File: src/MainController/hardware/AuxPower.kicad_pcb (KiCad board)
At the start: 2 copper layers, 90 x 90 mm, 123 parts, among them J1 MC 1,5/2, J10 MC 1,5/4, J11 S3B-XH-A, J12 S3B-XH-A, J13 S3B-XH-A, J14 S3B-XH-A, J15 S3B-XH-A, J16 B3B-XH-A, J17 B4B-XH-A, J2 MC 1,5/2, J3 MC 1,5/2, J4 MC 1,5/2, J5 MC 1,5/2, J6 MC 1,5/4, J7 MC 1,5/4, J8 MC 1,5/4, J9 MC 1,5/4, Q1 BC846B,235, Q10 AO4421, Q2 BC846B,235, Q3 BC846B,235, Q4 BC846B,235, Q5 BC846B,235, Q6 AO4421, Q7 AO4421, Q8 AO4421, Q9 AO4421, U1 ZXCT1009, U2 ZXCT1009, U3 ZXCT1009, U5 ZXCT1009, U6 PIC18F26K83, U7 PI4IOE5V6416, U8 MCP9701

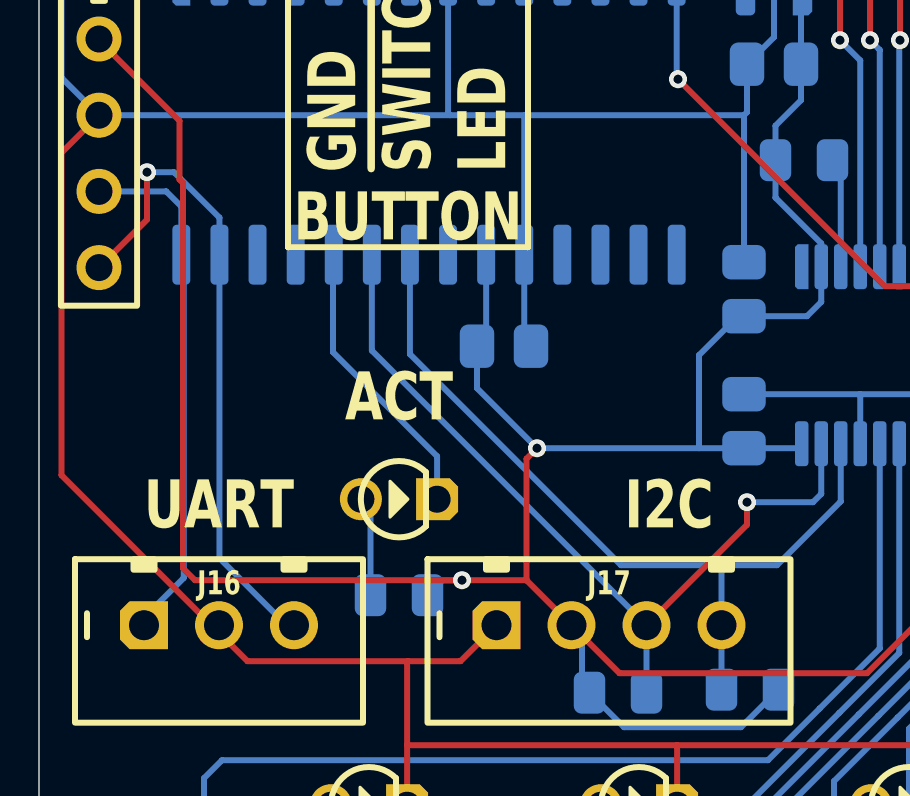
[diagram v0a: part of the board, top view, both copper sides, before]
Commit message: MainController: Moved Activity LED a bit
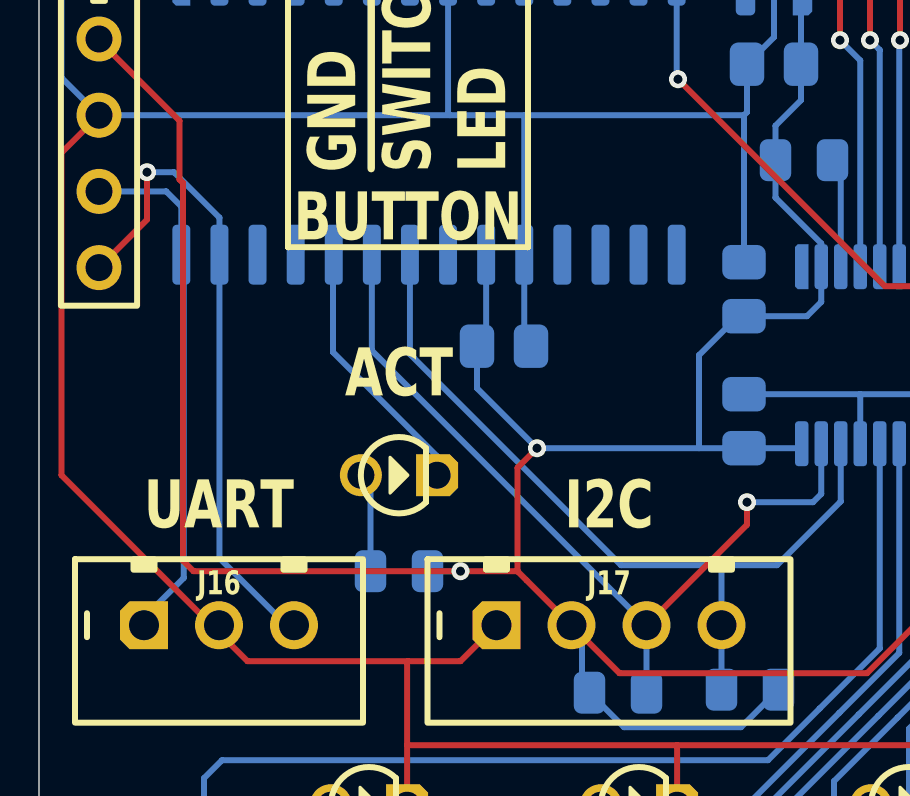
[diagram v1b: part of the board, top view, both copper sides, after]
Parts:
- moved DS12 0.80 mm to (27.0, 77.0)
- moved R32 0.80 mm to (27.0, 80.2)
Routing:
- net OUT_ACTIVITY: track 9.76 -> 8.76 mm
- net 5V: track 128.2 -> 127.6 mm
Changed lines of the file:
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@@
 	(footprint "Medo64:DS (D3.0)"
 		(layer "F.Cu")
-		(at 27 77.8 180)
+		(at 27 77 180)
 		(property "Reference" "DS12"
 			(at 0 -2.45 0)
@@
 	(footprint "Medo64:R (0805)"
 		(layer "B.Cu")
-		(at 27 81)
+		(at 27 80.2)
 		(tags "RESC2013X70N")
 		(property "Reference" "R32"
@@
 	)
 	(gr_text "ACT"
-		(at 27 74.4 0)
+		(at 27 73.6 0)
 		(layer "F.SilkS" knockout)
 		(effects
@@
 	)
 	(gr_text "I2C"
-		(at 36 78 0)
+		(at 34 78 0)
 		(layer "F.SilkS" knockout)
 		(effects
@@
 	)
 	(segment
-		(start 31.25 80.5)
-		(end 20.2 80.5)
+		(start 19.682462 67.142462)
+		(end 19.682462 65.182462)
 		(width 0.2)
 		(layer "F.Cu")
@@
 	)
 	(segment
-		(start 19.8 80.1)
-		(end 19.8 67.26)
+		(start 32.75 82)
+		(end 31.25 80.5)
 		(width 0.2)
 		(layer "F.Cu")
@@
 	)
 	(segment
-		(start 32.75 82)
-		(end 31.25 80.5)
+		(start 30.95 80.2)
+		(end 30.95 76.75)
 		(width 0.2)
 		(layer "F.Cu")
@@
 	)
 	(segment
-		(start 19.682462 67.142462)
-		(end 19.682462 65.182462)
+		(start 30.95 76.75)
+		(end 31.6 76.1)
 		(width 0.2)
 		(layer "F.Cu")
@@
 	)
 	(segment
-		(start 19.682462 65.182462)
-		(end 17 62.5)
+		(start 20.15 80.2)
+		(end 19.8 79.85)
 		(width 0.2)
 		(layer "F.Cu")
@@
 	)
 	(segment
-		(start 20.2 80.5)
-		(end 19.8 80.1)
+		(start 19.682462 65.182462)
+		(end 17 62.5)
 		(width 0.2)
 		(layer "F.Cu")
@@
 	)
 	(segment
-		(start 34.35 83.6)
-		(end 32.75 82)
+		(start 19.8 67.26)
+		(end 19.682462 67.142462)
 		(width 0.2)
 		(layer "F.Cu")
@@
 	)
 	(segment
-		(start 19.8 67.26)
-		(end 19.682462 67.142462)
+		(start 31.25 80.5)
+		(end 30.95 80.2)
 		(width 0.2)
 		(layer "F.Cu")
@@
 	)
 	(segment
-		(start 31.25 80.5)
-		(end 31.25 76.45)
+		(start 34.35 83.6)
+		(end 32.75 82)
+		(width 0.2)
+		(layer "F.Cu")
+		(net 75)
+	)
+	(segment
+		(start 30.95 80.2)
+		(end 20.15 80.2)
 		(width 0.2)
 		(layer "F.Cu")
@@
 	)
 	(segment
-		(start 31.25 76.45)
-		(end 31.6 76.1)
+		(start 19.8 79.85)
+		(end 19.8 67.26)
 		(width 0.2)
 		(layer "F.Cu")
@@
 	)
 	(via
-		(at 29.1 80.5)
+		(at 29.05 80.2)
 		(size 0.6)
 		(drill 0.3)
@@
 	)
 	(segment
-		(start 28.45 80.5)
-		(end 29.1 80.5)
-		(width 0.2)
-		(layer "B.Cu")
-		(net 75)
-	)
-	(segment
 		(start 33.35 84.25)
 		(end 34.5 85.4)
@@
 	)
 	(segment
-		(start 27.95 81)
-		(end 28.45 80.5)
-		(width 0.2)
-		(layer "B.Cu")
-		(net 75)
-	)
-	(segment
 		(start 52.6 74.8)
 		(end 52.6 71.8)
@@
 	)
 	(segment
+		(start 27.95 80.2)
+		(end 28.95 80.2)
+		(width 0.2)
+		(layer "B.Cu")
+		(net 75)
+	)
+	(segment
 		(start 29.6 72.7)
 		(end 29.6 74.1)
@@
 	)
 	(segment
+		(start 28.95 80.2)
+		(end 29.05 80.2)
+		(width 0.2)
+		(layer "B.Cu")
+		(net 75)
+	)
+	(segment
 		(start 31.6 76.1)
 		(end 37 76.1)
@@
 	)
 	(segment
-		(start 26.05 78.32)
-		(end 25.73 78)
+		(start 26.05 77.32)
+		(end 25.73 77)
 		(width 0.2)
 		(layer "B.Cu")
@@
 	)
 	(segment
-		(start 26.05 81)
-		(end 26.05 78.32)
+		(start 26.05 80.2)
+		(end 26.05 77.32)
 		(width 0.2)
 		(layer "B.Cu")
@@
 	)
 	(segment
-		(start 28.27 78)
-		(end 28.27 76.37)
+		(start 28.27 76.37)
+		(end 24.8 72.9)
 		(width 0.2)
 		(layer "B.Cu")
@@
 	)
 	(segment
-		(start 28.27 76.37)
-		(end 24.8 72.9)
+		(start 28.27 77)
+		(end 28.27 76.37)
 		(width 0.2)
 		(layer "B.Cu")

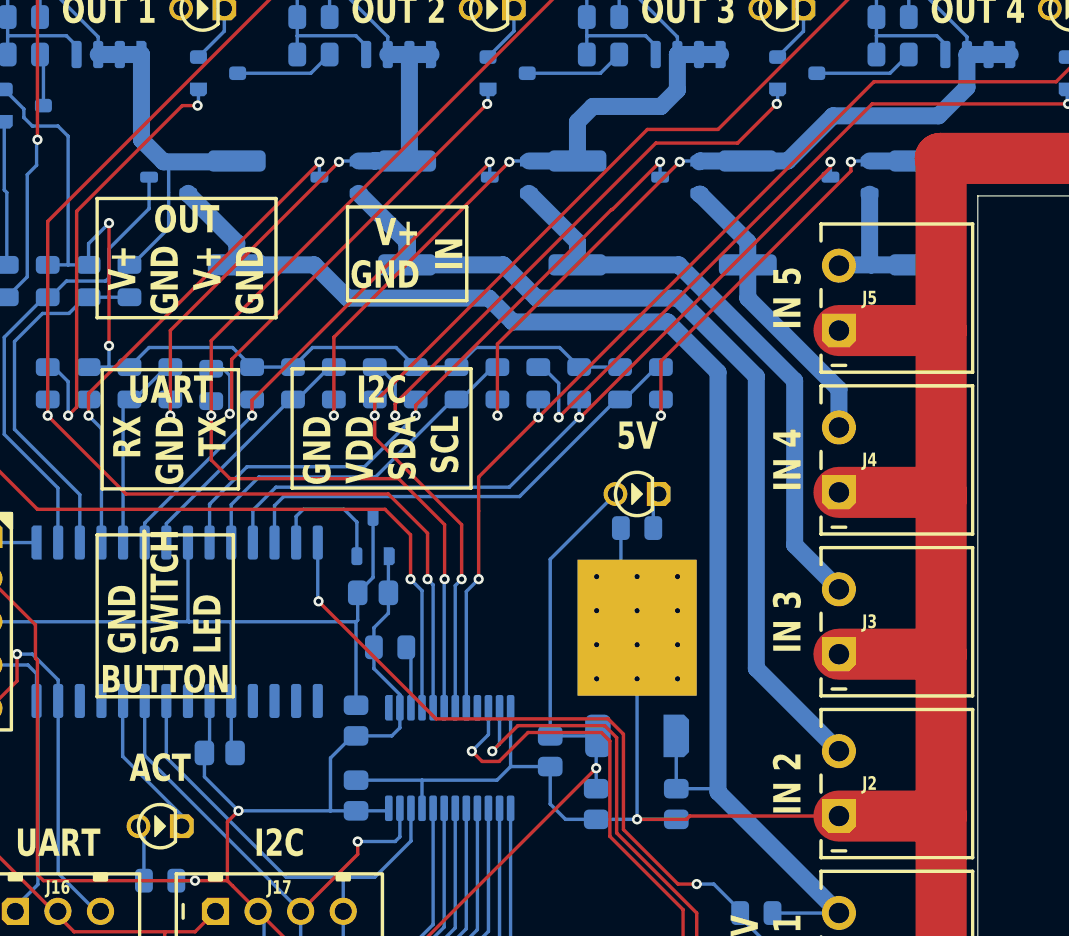
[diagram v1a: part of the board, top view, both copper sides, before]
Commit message: MainController: Adding forgotten 1K to GND for current monitor
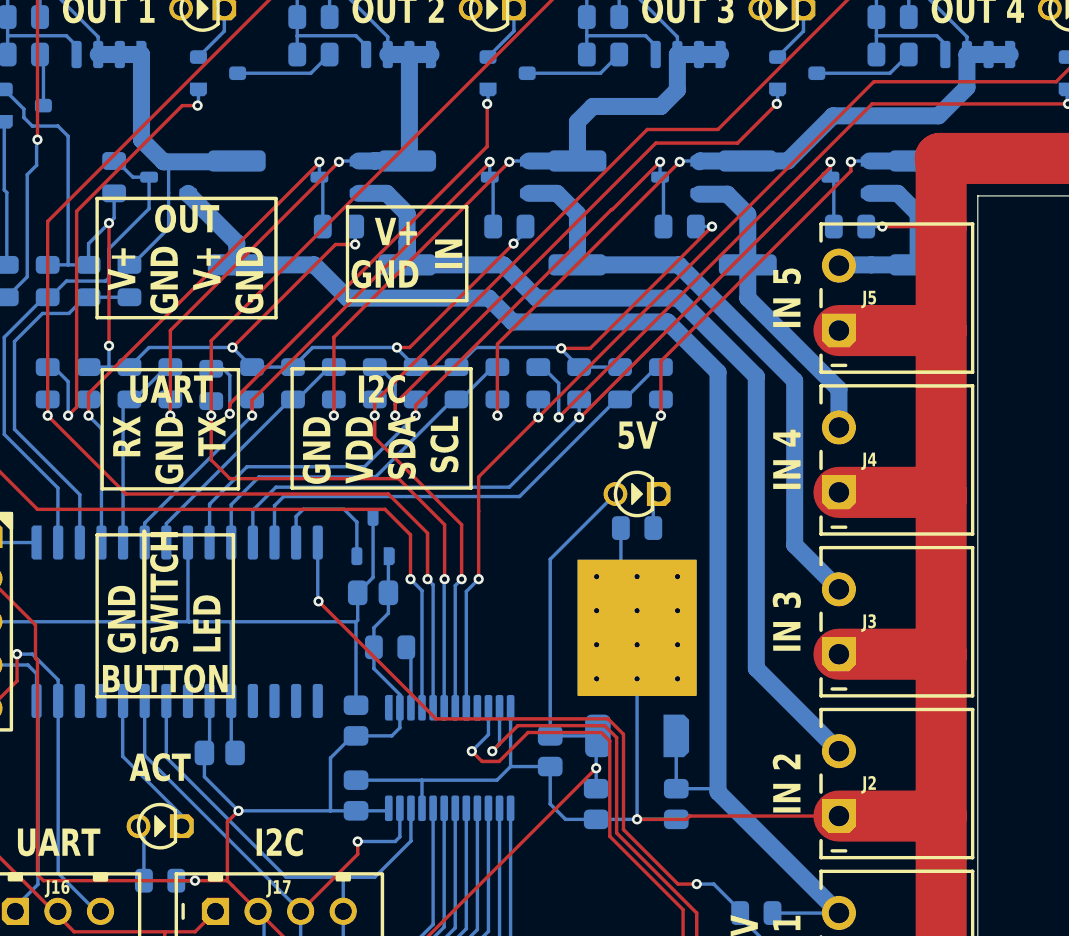
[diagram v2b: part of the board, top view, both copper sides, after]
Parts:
- added R34: 1K, Medo64:R (0805), B.Cu at (67.5, 41.8)
- added R35: 1K, Medo64:R (0805), B.Cu at (57.5, 41.8)
- added R36: 1K, Medo64:R (0805), B.Cu at (47.5, 41.8)
- added R37: 1K, Medo64:R (0805), B.Cu at (37.5, 41.8)
- added R38: 1K, Medo64:R (0805), B.Cu at (24.3, 38.9)
- renumbered R34 to R39, R35 to R40, R36 to R41, R37 to R42, R38 to R43, R39 to R44, R40 to R45, R41 to R46, R42 to R47, R43 to R48, R44 to R49, R45 to R50, R46 to R51, R47 to R52, R48 to R53, R49 to R54, R50 to R55, R51 to R56, R52 to R57, R53 to R58, R54 to R59, R55 to R60, R56 to R61, R57 to R62, R58 to R63, R59 to R64, R60 to R65, R61 to R66, R62 to R67
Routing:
- net GND: track 708.9 -> 749.1 mm, vias 3 -> 10
- net INPUT3: track 39.1 -> 36.1 mm
- net ADC_CURRENT2: track 30.1 -> 32.8 mm
- net ADC_CURRENT5: track 46.4 -> 49.1 mm
- net ADC_CURRENT3: track 32.6 -> 35.3 mm
- net ADC_CURRENT4: track 39.2 -> 41.9 mm
- net ADC_CURRENT1: track 27.5 -> 29.8 mm
- net INPUT5: track 8.80 -> 11.0 mm
- net INPUT2: track 53.4 -> 54.4 mm
- net INPUT4: track 17.1 -> 18.1 mm

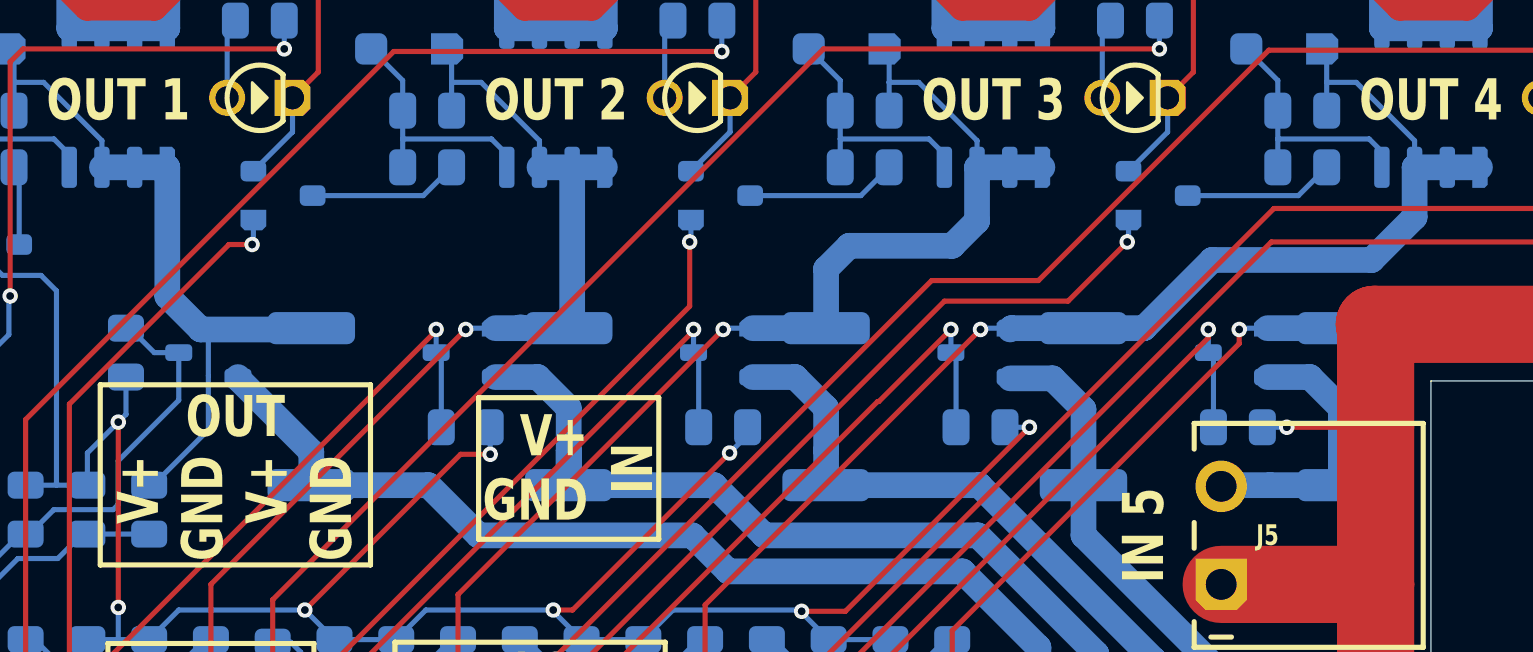
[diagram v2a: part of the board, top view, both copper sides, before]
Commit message: MainController: adjusting trace widths a bit
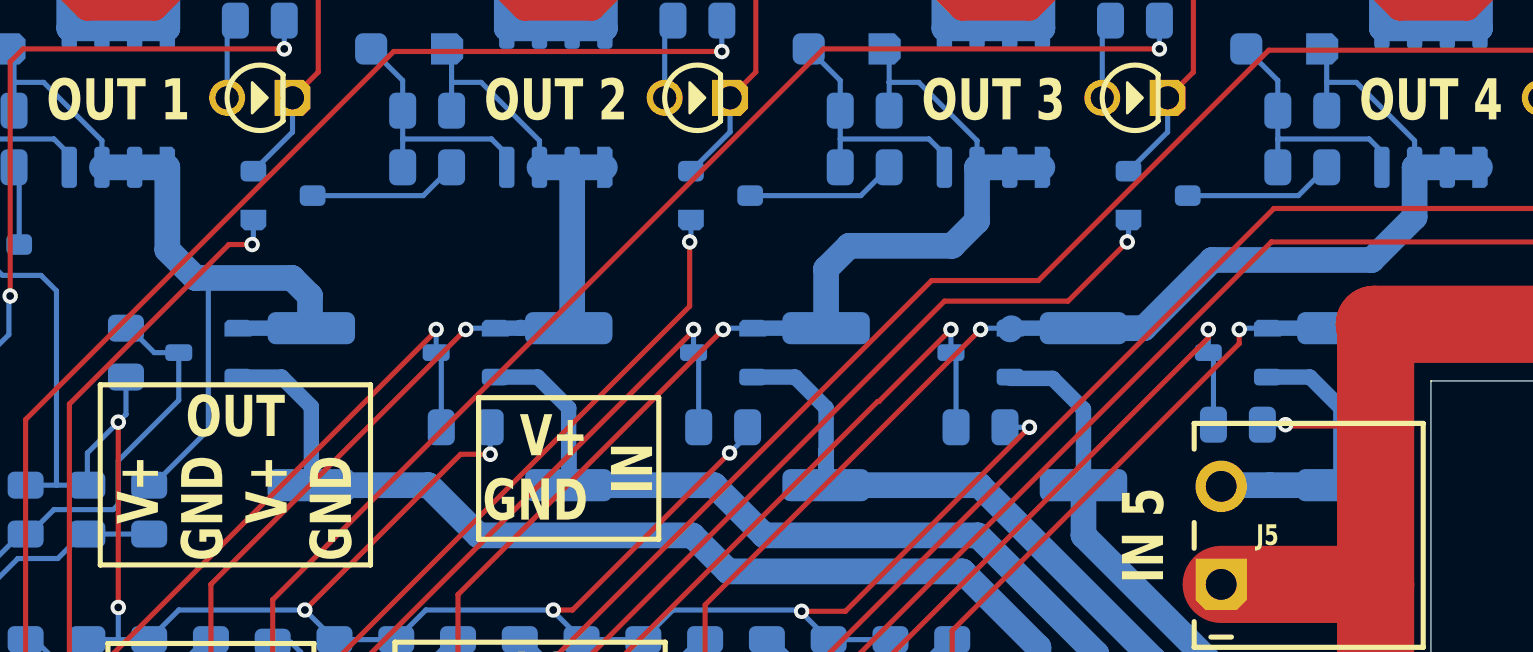
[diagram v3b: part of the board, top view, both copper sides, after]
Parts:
- moved R34 0.10 mm to (67.5, 41.7)
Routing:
- net INPUT1': track 28.2 -> 32.6 mm
- net INPUT1: track 80.5 -> 81.4 mm
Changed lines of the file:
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@@
 	(footprint "Medo64:R (0805)"
 		(layer "B.Cu")
-		(at 67.5 41.8)
+		(at 67.5 41.7)
 		(tags "RESC2013X70N")
 		(property "Reference" "R34"
@@
 	)
 	(segment
+		(start 72.85 41.75)
+		(end 69.400003 41.75)
+		(width 0.2)
+		(layer "F.Cu")
+		(net 1)
+	)
+	(segment
 		(start 48.77 28)
 		(end 48.77 23.055)
@@
 	)
 	(segment
-		(start 69.4 41.8)
-		(end 72.8 41.8)
-		(width 0.2)
-		(layer "F.Cu")
-		(net 1)
-	)
-	(segment
 		(start 45.27 86)
 		(end 45.27 88)
@@
 	)
 	(segment
-		(start 72.8 41.8)
-		(end 72.85 41.75)
-		(width 0.2)
-		(layer "F.Cu")
-		(net 1)
-	)
-	(segment
 		(start 82.715 17)
 		(end 82.715 23)
@@
 	)
 	(segment
+		(start 69.400003 41.75)
+		(end 69.350006 41.700003)
+		(width 0.2)
+		(layer "F.Cu")
+		(net 1)
+	)
+	(segment
 		(start 72.85 47.905)
 		(end 66.85 47.905)
@@
 	)
 	(via
-		(at 69.4 41.8)
+		(at 69.350006 41.700003)
 		(size 0.6)
 		(drill 0.3)
@@
 	)
 	(segment
+		(start 69.350003 41.7)
+		(end 69.350006 41.700003)
+		(width 0.2)
+		(layer "B.Cu")
+		(net 1)
+	)
+	(segment
 		(start 20.4 44.05)
 		(end 21.6 44.05)
@@
 	)
 	(segment
-		(start 68.45 41.8)
-		(end 69.4 41.8)
-		(width 0.2)
-		(layer "B.Cu")
-		(net 1)
-	)
-	(segment
 		(start 55 68.35)
 		(end 55 66.35)
@@
 	)
 	(segment
+		(start 68.45 41.7)
+		(end 69.350003 41.7)
+		(width 0.2)
+		(layer "B.Cu")
+		(net 1)
+	)
+	(segment
 		(start 22.8 50.05)
 		(end 24 50.05)
@@
 	)
 	(segment
+		(start 30.35 39.85)
+		(end 31.5 41)
+		(width 0.6)
+		(layer "B.Cu")
+		(net 37)
+	)
+	(segment
+		(start 31.5 41)
+		(end 31.5 44.05)
+		(width 0.6)
+		(layer "B.Cu")
+		(net 37)
+	)
+	(segment
 		(start 57.3 74.8)
 		(end 57.3 71.7)
@@
 	)
 	(segment
-		(start 28.65 39.85)
-		(end 28.65 39.9)
-		(width 1)
-		(layer "B.Cu")
-		(net 37)
-	)
-	(segment
 		(start 62.95 82.1)
 		(end 66.845 82.1)
@@
 	)
 	(segment
-		(start 28.65 39.9)
-		(end 31.5 42.75)
-		(width 1)
+		(start 28.65 39.85)
+		(end 30.35 39.85)
+		(width 0.6)
 		(layer "B.Cu")
 		(net 37)
@@
 	)
 	(segment
-		(start 31.5 42.75)
-		(end 31.5 44.05)
-		(width 1)
-		(layer "B.Cu")
-		(net 37)
-	)
-	(segment
 		(start 56.8 47.4)
 		(end 59.75 50.35)
@@
 	)
 	(segment
-		(start 27.5 39.8)
-		(end 27.5 38.3)
+		(start 27.5 41.9)
+		(end 27.5 36.05)
 		(width 0.2)
 		(layer "B.Cu")
@@
 	)
 	(segment
-		(start 19.95 28.4)
-		(end 19.95 27.375)
-		(width 0.2)
+		(start 25.905 31.7)
+		(end 25.905 34.905)
+		(width 1)
 		(layer "B.Cu")
 		(net 38)
 	)
 	(segment
-		(start 24.635 31.7)
-		(end 23.365 31.7)
-		(width 1)
+		(start 31.5 37.95)
+		(end 28.65 37.95)
+		(width 0.6)
 		(layer "B.Cu")
 		(net 38)
 	)
 	(segment
-		(start 25.905 31.7)
-		(end 25.905 36.705)
+		(start 31.45 36.7)
+		(end 31.45 38)
 		(width 1)
 		(layer "B.Cu")
@@
 	)
 	(segment
-		(start 27.2 38)
-		(end 31.45 38)
-		(width 1)
+		(start 19.95 28.4)
+		(end 19.95 27.375)
+		(width 0.2)
 		(layer "B.Cu")
 		(net 38)
 	)
 	(segment
-		(start 25.35 44.05)
-		(end 27.5 41.9)
-		(width 0.2)
+		(start 24.635 31.7)
+		(end 23.365 31.7)
+		(width 1)
 		(layer "B.Cu")
 		(net 38)
 	)
 	(segment
-		(start 27.5 38.3)
-		(end 27.2 38)
-		(width 0.2)
+		(start 25.905 34.905)
+		(end 27 36)
+		(width 1)
 		(layer "B.Cu")
 		(net 38)
 	)
 	(segment
-		(start 27.5 41.9)
-		(end 27.5 39.8)
-		(width 0.2)
+		(start 30.75 36)
+		(end 31.45 36.7)
+		(width 1)
 		(layer "B.Cu")
 		(net 38)
@@
 	)
 	(segment
-		(start 25.905 36.705)
-		(end 27.2 38)
+		(start 25.35 44.05)
+		(end 27.5 41.9)
+		(width 0.2)
+		(layer "B.Cu")
+		(net 38)
+	)
+	(segment
+		(start 27 36)
+		(end 30.75 36)
 		(width 1)
 		(layer "B.Cu")
@@
 		(start 39.6 37.95)
 		(end 41.5 37.95)
-		(width 1)
+		(width 0.6)
 		(layer "B.Cu")
 		(net 39)
@@
 		(start 39.635 37.915)
 		(end 39.6 37.95)
-		(width 1)
+		(width 0.6)
 		(layer "B.Cu")
 		(net 39)
@@
 		(start 38.65 37.95)
 		(end 39.6 37.95)
-		(width 1)
+		(width 0.6)
 		(layer "B.Cu")
 		(net 39)
@@
 		(start 40.3 39.85)
 		(end 38.65 39.85)
-		(width 1)
+		(width 0.6)
 		(layer "B.Cu")
 		(net 40)
@@
 		(start 41.5 41.05)
 		(end 40.3 39.85)
-		(width 1)
+		(width 0.6)
 		(layer "B.Cu")
 		(net 40)
@@
 		(start 41.5 42.7)
 		(end 41.5 41.05)
-		(width 1)
+		(width 0.6)
 		(layer "B.Cu")
 		(net 40)
@@
 		(start 41.5 43.55)
 		(end 41.5 42.7)
-		(width 1)
+		(width 0.6)
 		(layer "B.Cu")
 		(net 40)
@@
 		(start 41.5 42.7)
 		(end 41.5 44.05)
-		(width 1)
+		(width 0.6)
 		(layer "B.Cu")
 		(net 40)
@@
 		(start 51.5 44.05)
 		(end 51.5 42.7)
-		(width 1)
+		(width 0.6)
 		(layer "B.Cu")
 		(net 41)
@@
 		(start 50.3 39.85)
 		(end 48.65 39.85)
-		(width 1)
+		(width 0.6)
 		(layer "B.Cu")
 		(net 41)
@@
 		(start 51.5 42.7)
 		(end 51.5 41.05)
-		(width 1)
+		(width 0.6)
 		(layer "B.Cu")
 		(net 41)
@@
 		(start 51.5 43.55)
 		(end 51.5 42.7)
-		(width 0.2)
+		(width 0.6)
 		(layer "B.Cu")
 		(net 41)
@@
 		(start 51.5 41.05)
 		(end 50.3 39.85)
-		(width 1)
+		(width 0.6)
 		(layer "B.Cu")
 		(net 41)
@@
 		(start 48.65 37.95)
 		(end 51.5 37.95)
-		(width 1)
+		(width 0.6)
 		(layer "B.Cu")
 		(net 42)
@@
 		(start 60.3 39.9)
 		(end 61.5 41.1)
-		(width 1)
+		(width 0.6)
 		(layer "B.Cu")
 		(net 43)
@@
 		(start 61.5 41.1)
 		(end 61.5 44.05)
-		(width 1)
+		(width 0.6)
 		(layer "B.Cu")
 		(net 43)
@@
 		(start 58.65 39.9)
 		(end 60.3 39.9)
-		(width 1)
+		(width 0.6)
 		(layer "B.Cu")
 		(net 43)
@@
 		(start 61.5 37.95)
 		(end 58.7 37.95)
-		(width 1)
+		(width 0.6)
 		(layer "B.Cu")
 		(net 44)
@@
 		(start 70.3 39.85)
 		(end 68.65 39.85)
-		(width 1)
+		(width 0.6)
 		(layer "B.Cu")
 		(net 45)
@@
 		(start 71.5 44.05)
 		(end 71.5 41.05)
-		(width 1)
+		(width 0.6)
 		(layer "B.Cu")
 		(net 45)
@@
 		(start 71.5 41.05)
 		(end 70.3 39.85)
-		(width 1)
+		(width 0.6)
 		(layer "B.Cu")
 		(net 45)
@@
 		(start 71.5 37.95)
 		(end 68.649998 37.95)
-		(width 1)
+		(width 0.6)
 		(layer "B.Cu")
 		(net 46)
